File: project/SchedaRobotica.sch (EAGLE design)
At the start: 73 parts, among them IC1 LMZ14202TZE-ADJ_NOPB, IC2 VNH7070ASTR, IC3 VNH7070ASTR, IC4 VNH7070ASTR, IC5 VNH7070ASTR, M1 43650-0201, M2 43650-0201, M3 43650-0201, M4 43650-0201

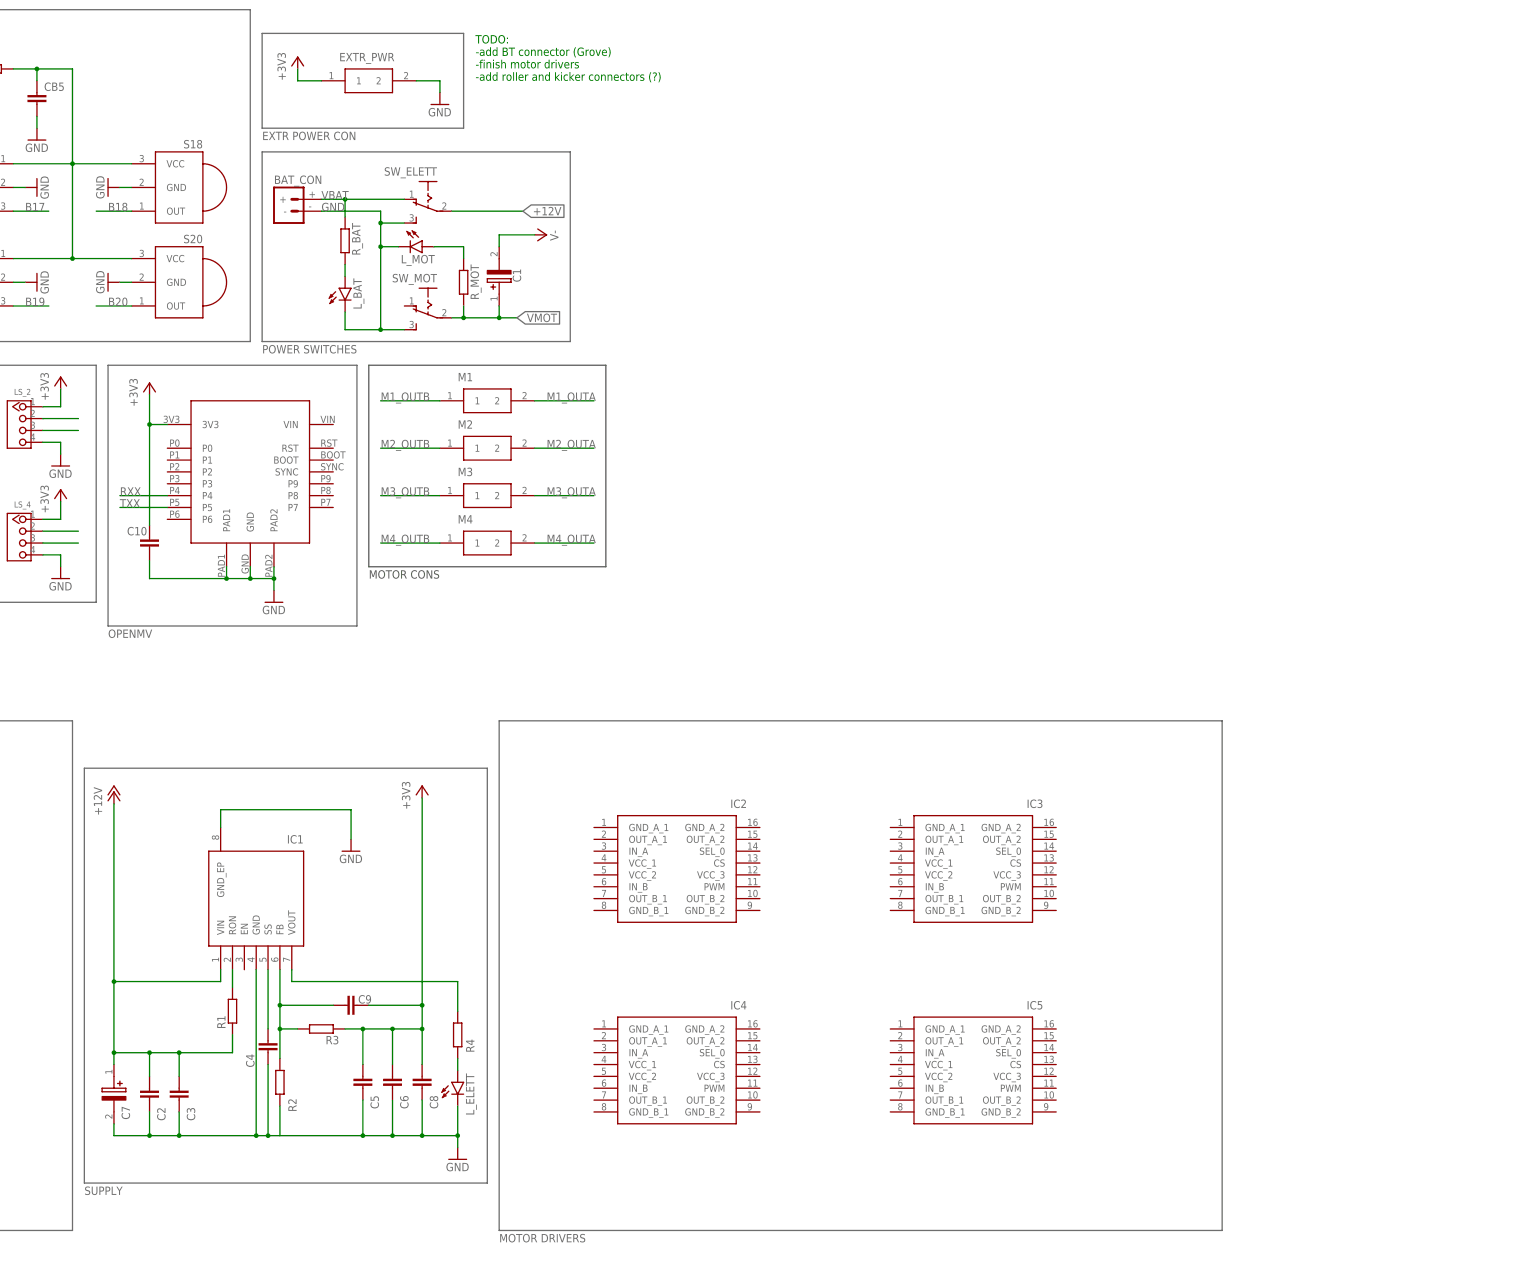
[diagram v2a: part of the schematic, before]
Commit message: added motor drivers, found a problem in brd creation tho :c
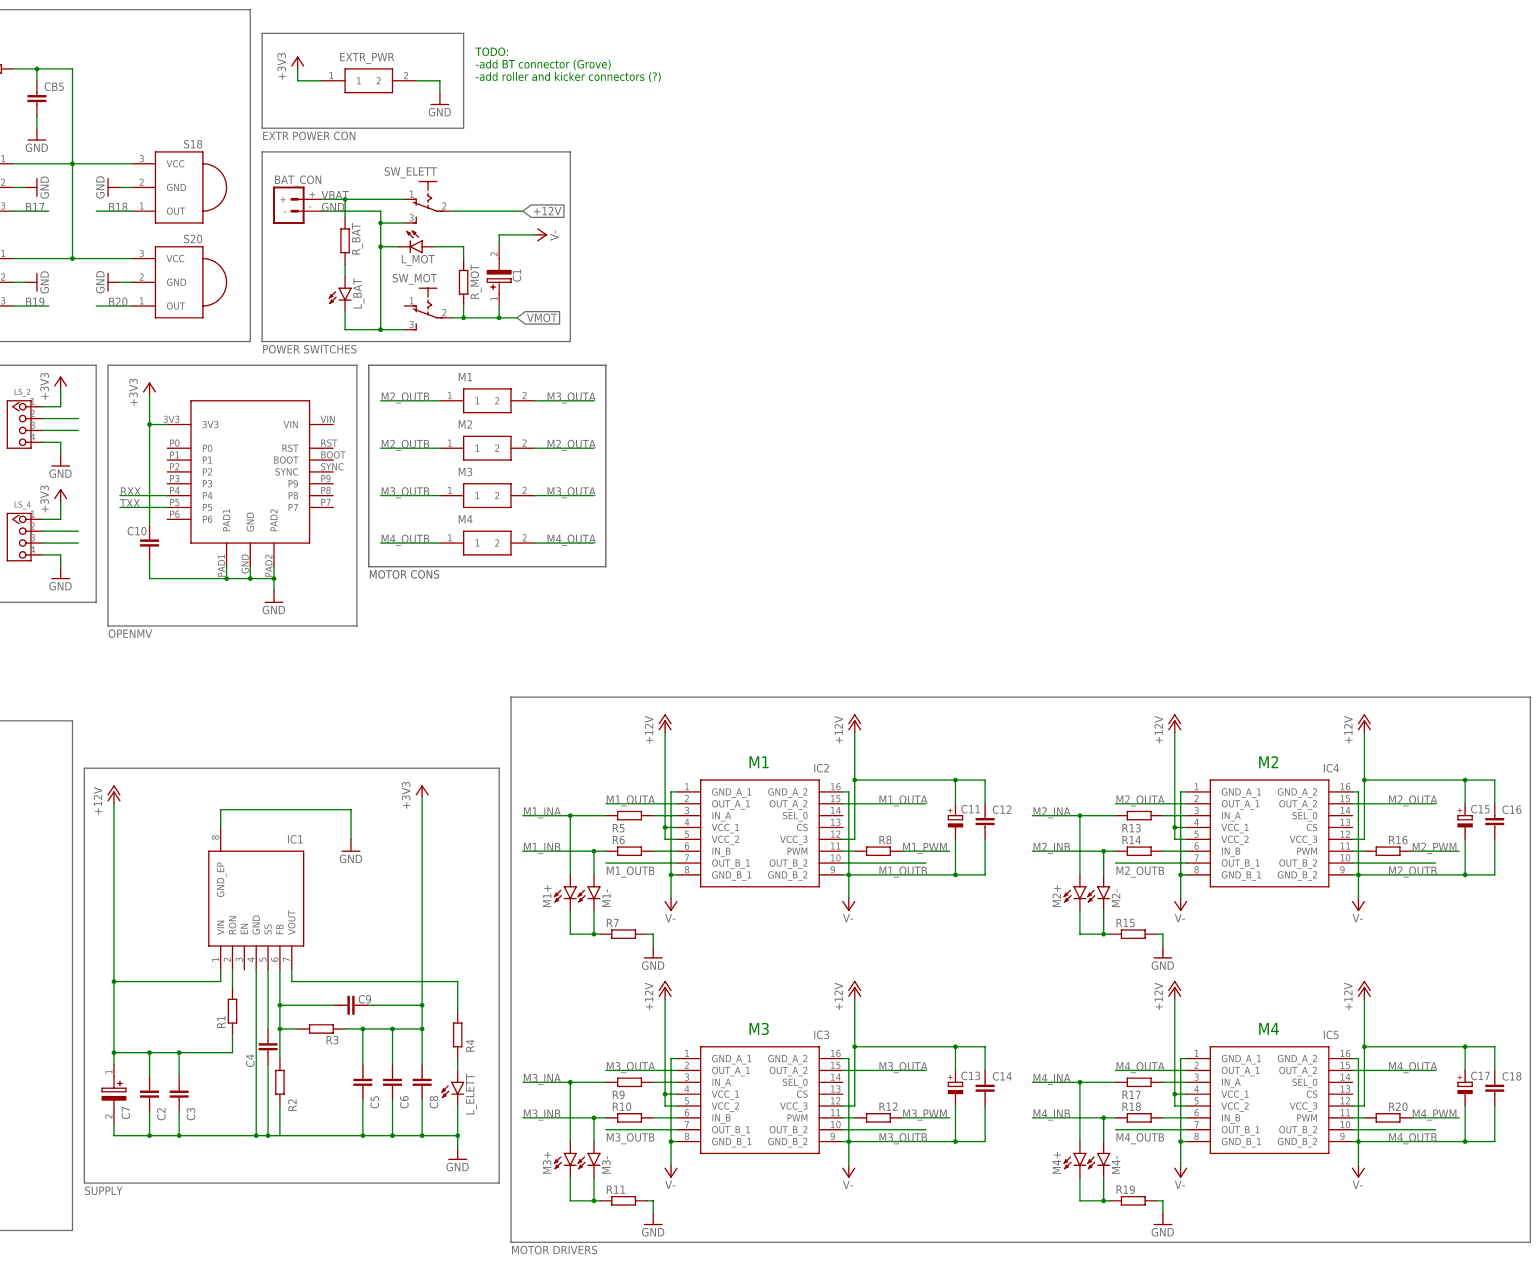
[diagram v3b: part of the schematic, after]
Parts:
- added C11, C13, C15, C17: (no value), rcl:CPOL-EUE
- added C12, C14, C16, C18: (no value), rcl:C-EUC0805
- added M1+, M1-, M2+, M2-, M3+, M3-, M4+, M4-: (no value), led:LEDCHIPLED_1206
- added R10, R11, R12, R13, R14, R15, R16, R17, R18, R19, R20, R5, R6, R7, R8, R9: (no value), rcl:R-EU_M0805
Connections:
- new net M1_INA: M1+.A, R5.1
- new net M1_INB: M1-.A, R6.1
- new net M1_PWM: R8.2
- new net M2_INA: M2+.A, R13.1
- new net M2_INB: M2-.A, R14.1
- new net M2_PWM: R16.2
- new net M3_INA: M3+.A, R9.1
- new net M3_INB: M3-.A, R10.1
- new net M3_PWM: R12.2
- new net M4_INA: M4+.A, R17.1
- new net M4_INB: M4-.A, R18.1
- new net M4_PWM: R20.2
- new net N$21: M1+.C, M1-.C, R7.1
- new net N$22: IC2.IN_A, R5.2
- new net N$23: IC2.IN_B, R6.2
- new net N$24: IC2.PWM, R8.1
- new net N$25: IC3.IN_A, R9.2
- new net N$26: IC3.IN_B, R10.2
- new net N$27: M3+.C, M3-.C, R11.1
- new net N$28: IC3.PWM, R12.1
- new net N$29: IC4.IN_A, R13.2
- new net N$30: IC4.IN_B, R14.2
- new net N$31: M2+.C, M2-.C, R15.1
- new net N$32: IC4.PWM, R16.1
- new net N$33: IC5.IN_A, R17.2
- new net N$34: IC5.IN_B, R18.2
- new net N$35: M4+.C, M4-.C, R19.1
- new net N$36: IC5.PWM, R20.1
- net +12V: now also C11.+, C12.1, C13.+, C14.1, C15.+, C16.1, C17.+, C18.1, IC2.VCC_1, IC2.VCC_2, IC2.VCC_3, IC3.VCC_1, IC3.VCC_2, IC3.VCC_3, IC4.VCC_1, IC4.VCC_2, IC4.VCC_3, IC5.VCC_1, IC5.VCC_2, IC5.VCC_3
- net GND: now also R11.2, R15.2, R19.2, R7.2
- net M1_OUTA: now also IC2.OUT_A_1, IC2.OUT_A_2; no longer M1.2
- net M1_OUTB: now also IC2.OUT_B_1, IC2.OUT_B_2; no longer M1.1
- net M2_OUTA: now also IC4.OUT_A_1, IC4.OUT_A_2
- net M2_OUTB: now also IC4.OUT_B_1, IC4.OUT_B_2, M1.1
- net M3_OUTA: now also IC3.OUT_A_1, IC3.OUT_A_2, M1.2
- net M3_OUTB: now also IC3.OUT_B_1, IC3.OUT_B_2
- net M4_OUTA: now also IC5.OUT_A_1, IC5.OUT_A_2
- net M4_OUTB: now also IC5.OUT_B_1, IC5.OUT_B_2
- net V-: now also C11.-, C12.2, C13.-, C14.2, C15.-, C16.2, C17.-, C18.2, IC2.GND_A_1, IC2.GND_A_2, IC2.GND_B_1, IC2.GND_B_2, IC3.GND_A_1, IC3.GND_A_2, IC3.GND_B_1, IC3.GND_B_2, IC4.GND_A_1, IC4.GND_A_2, IC4.GND_B_1, IC4.GND_B_2, IC5.GND_A_1, IC5.GND_A_2, IC5.GND_B_1, IC5.GND_B_2
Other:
- note added: "M1"
- note added: "M2"
- note added: "M3"
- note added: "M4"
- note added: "TODO: -add BT connector (Grove) -add roller and kicker connectors (?)"
- note removed: "TODO: -add BT connector (Grove) -finish motor drivers -add roller and kicker connectors (?)"
- moved on the sheet: IC2, IC3, IC4, IC5

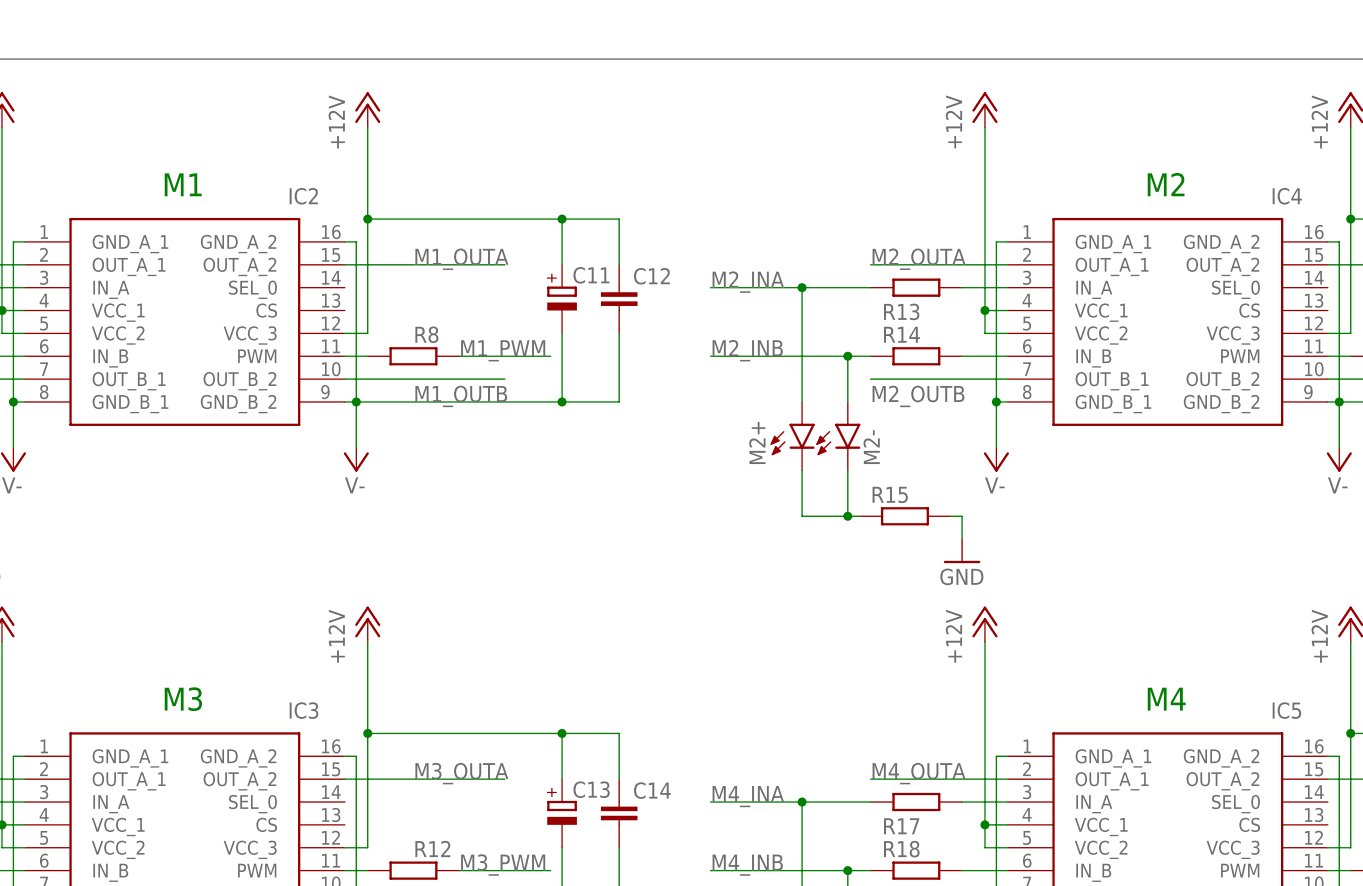
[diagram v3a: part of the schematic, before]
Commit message: created the array of ball sensors, now to understand how to rotate them right, implementing a custom made IMU lbr
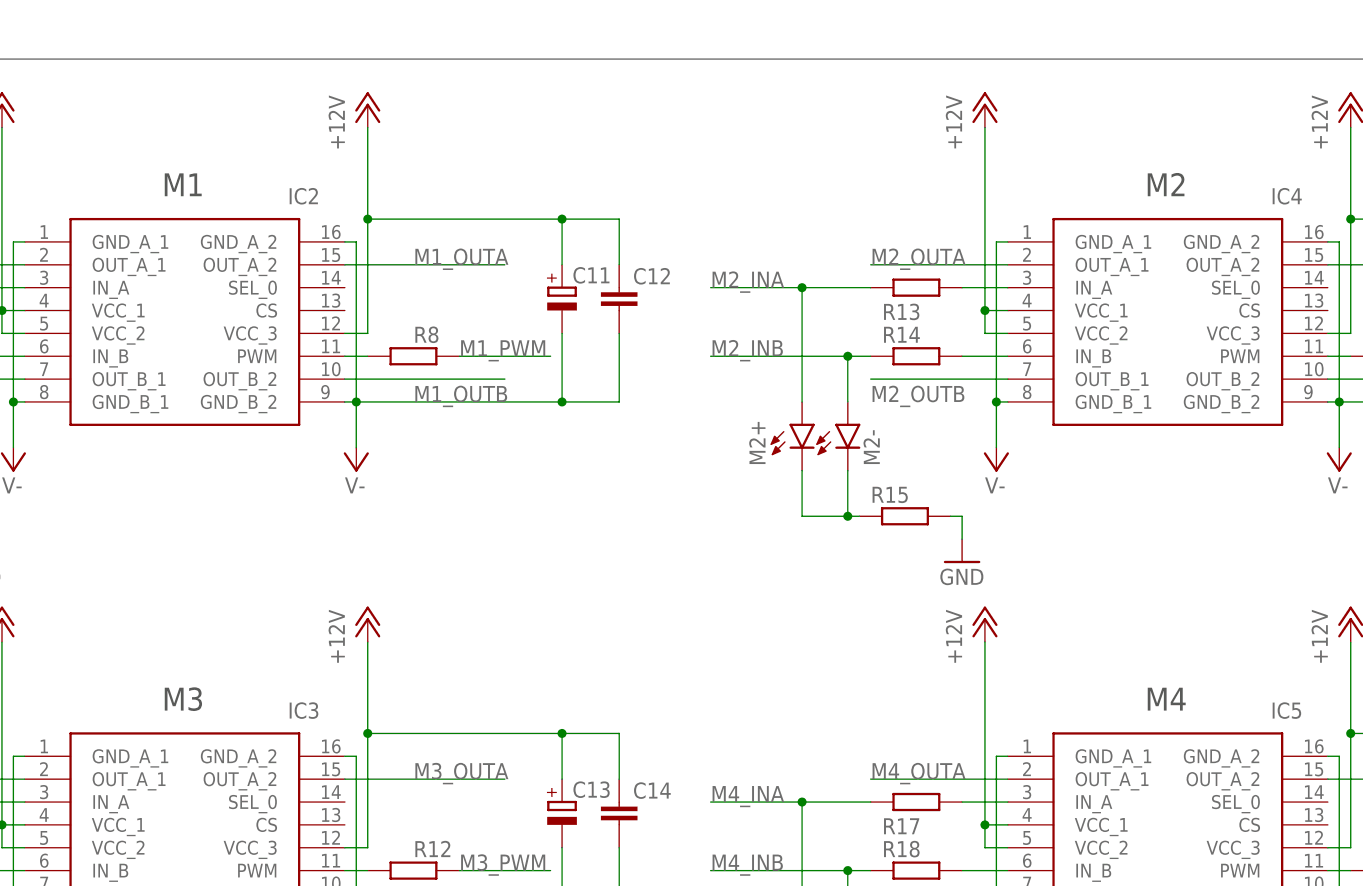
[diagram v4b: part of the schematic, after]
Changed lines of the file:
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@@
 <setting verticaltext="up"/>
 </settings>
-<grid distance="0.1" unitdist="inch" unit="mil" style="dots" multiple="1" display="yes" altdistance="50" altunitdist="mil" altunit="mil"/>
+<grid distance="0.1" unitdist="inch" unit="inch" style="lines" multiple="1" display="no" altdistance="0.01" altunitdist="inch" altunit="inch"/>
 <layers>
 <layer number="1" name="Top" color="4" fill="1" visible="no" active="no"/>
@@
 -add BT connector (Grove)
 -add roller and kicker connectors (?)</text>
-<text x="340.36" y="101.6" size="2.54" layer="91">M1</text>
-<text x="449.58" y="101.6" size="2.54" layer="91">M2</text>
-<text x="340.36" y="44.45" size="2.54" layer="91">M3</text>
-<text x="449.58" y="44.45" size="2.54" layer="91">M4</text>
+<text x="340.36" y="101.6" size="2.54" layer="97">M1</text>
+<text x="449.58" y="101.6" size="2.54" layer="97">M2</text>
+<text x="340.36" y="44.45" size="2.54" layer="97">M3</text>
+<text x="449.58" y="44.45" size="2.54" layer="97">M4</text>
 </plain>
 <instances>
